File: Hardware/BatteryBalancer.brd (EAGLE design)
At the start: 49 parts, among them J2 ICSP, U3 SINGLECELL, U4 ATMEGA328P_TQFP, U5 SINGLECELL, U6 SINGLECELL, U7 SINGLECELL, Y1 16MHz

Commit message: Going home
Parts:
- removed JP10: JP10, SparkFun-Connectors:1X08_SMD_COMBINED
- removed JP11: IOL, SparkFun-Connectors:1X08_SMD_COMBINED
- removed JP13: AD, SparkFun-Connectors:1X06_SMD_STRAIGHT_COMBO
- removed U3, U5, U6, U7: SINGLECELL, BBLib:1X02_SMD_0.1IN
- added C11, C12, C13, C14, C18: 0.1uF, SparkFun-Capacitors:0603
- added C15: 10uF, SparkFun-Capacitors:EIA3216
- added C17: 10nF, SparkFun-Capacitors:0603
- added D2: GREEN, SparkFun-LED:LED-1206
- added D3: YELLOW, SparkFun-LED:LED-1206-HIDDENSILK
- added F1: 6V 0.5A, SparkFun-Fuses:0805
- added J1: (no value), SparkFun-Connectors:USB-MICROB-PTH-MILL
- added LED1: Blue, SparkFun-LED:LED-1206-HIDDENSILK
- added R1, R24: 10k, SparkFun-Resistors:0603
- added R25, R26: 4.7k, SparkFun-Resistors:0603
- added U1: CH340C, SparkFun-IC-Comms:SO016
- added U10, U11, U2, U8, U9: TAP_POINT, BBLib:1X01_SMD_0.1IN
- J2: value ICSP -> ISP
- R3: value 10k -> 4.7k
- S1: value RESET -> Tall Switch; device SparkFun-Electromechanical:TACTILE-SWITCH-SMD -> SparkFun-Switches:TACTILE_SWITCH_SMD_5.2MM
- moved S1 249.6 mm to (-80.6, -298.2)
- moved R3 249.5 mm to (-82.7, -307.2)
- moved U4 247.3 mm to (-79.4, -261.5)
- moved Y1 245.6 mm to (-60.8, -296.8)
- moved C2 241.5 mm to (-69.7, -303.4)
- moved J2 229.0 mm to (-2.54, -323.9)
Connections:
- removed net 3.3V: JP10.5A, JP10.5B
- removed net 5V: C2.2, J2.2, JP10.4A, JP10.4B, JP10.7A, JP10.7B, R3.2, U4.18, U4.4, U4.6
- removed net AD0: JP13.1A, JP13.1B, U4.23
- removed net AD1: JP13.2A, JP13.2B, U4.24
- removed net AD2: JP13.3A, JP13.3B, U4.25
- removed net AD3: JP13.4A, JP13.4B, U4.26
- removed net AD4/SDA: JP13.5A, JP13.5B, U4.27
- removed net AD5/SCL: JP13.6A, JP13.6B, U4.28
- removed net IO2: JP11.3A, JP11.3B, U4.32
- removed net IO3: JP11.4A, JP11.4B, U4.1
- removed net IO4: JP11.5A, JP11.5B, U4.2
- removed net IO5: JP11.6A, JP11.6B, U4.9
- removed net IO6: JP11.7A, JP11.7B, U4.10
- removed net IO7: JP11.8A, JP11.8B, U4.11
- removed net IO8: U4.12
- removed net IO9: U4.13
- removed net VIN: JP10.1A, JP10.1B
- new net !DTR: C12.1, U1.13
- new net !PD: R1.1, U$2.15
- new net AREF: C2.1, U4.20
- new net D+: J1.D+, U1.5
- new net D-: J1.D-, U1.6
- new net N$1: LED1.A, R3.2
- new net N$36: D3.A, R25.1
- new net SHLD: J1.SHIELD, J1.SHIELD10, J1.SHIELD2, J1.SHIELD3, J1.SHIELD4, J1.SHIELD5, J1.SHIELD6, J1.SHIELD7, J1.SHIELD8, J1.SHIELD9
- new net USBVCC: C14.1, C15.+, F1.2
- new net VBATT: R16.2, R2.2, R7.1, U$2.16, U11.1
- new net VCC: C11.2, C18.1, J2.2, R24.2, R25.2, R26.2, U1.16, U4.18, U4.4, U4.6
- new net VUSB: C13.1, F1.1, J1.VBUS
- net GND: now also C11.1, C13.2, C14.2, C15.-, C17.2, C18.2, C2.2, J1.GND, LED1.C, U1.1, U2.1; no longer C2.1, JP10.2A, JP10.2B, JP10.3A, JP10.3B, U7.1
- net N$10: now also U8.1; no longer U6.1, U7.2
- net N$2: now also D2.A, R26.1; no longer R16.2, R2.2, R7.1, U$2.16, U5.2
- net N$23: now also R1.2
- net N$38: now also C17.1, U1.4; no longer U$2.15
- net N$6: now also U10.1; no longer U3.2, U5.1
- net N$8: now also U9.1; no longer U3.1, U6.2
- net RESET: now also C12.2, R24.1; no longer JP10.6A, JP10.6B, R3.1
- net RX-I: now also D3.C, U1.2; no longer JP11.1A, JP11.1B
- net SCLK: now also R3.1
- net TX-O: now also D2.C, U1.3; no longer JP11.2A, JP11.2B
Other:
- board outline added: 6.2 x 4.2 mm

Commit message: going home
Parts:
- added C16: 10uF, SparkFun-Capacitors:EIA3216
- added C19: 0.1uF, SparkFun-Capacitors:0603
- added C20: 47uF, SparkFun-Capacitors:PANASONIC_D
- added D1: TH, SparkFun-DiscreteSemi:SOT23-3
- added D4: MATCH, SparkFun-DiscreteSemi:SOT23-3
- added IC1: OP-AMP, SparkFun-IC-Amplifiers:SO08
- added IC3: LM1117, Testing:SOT223-ALT1
- added Q4: (no value), MTAES_V2_UniqueParts:SOT23-3
- added Q5: 4.3A/20V/54mΩ, SparkFun-DiscreteSemi:SOT23-3
- added R27: 1M, SparkFun-Resistors:0603
- added R28: 330k, SparkFun-Resistors:0603
- added R29: 715, SparkFun-Resistors:0603
- added R30: 240, SparkFun-Resistors:0603
- moved FRAME1 56.1 mm to (-67.3, -40.4)
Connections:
- removed net VBATT: R16.2, R2.2, R7.1, U$2.16, U11.1
- new net 5V: C16.+, C19.1, IC3.2, IC3.4, R30.2
- new net CHARGE: IC1.1
- new net N$39: IC3.1, R29.2, R30.1
- new net N$40: D4.3, IC1.3, R27.1
- new net N$41: D1.3, IC1.2, R28.1
- new net V_BATT: C20.+, IC1.8, IC3.3, Q5.2, R27.2, R28.2
- new net V_RAW: Q5.3, R16.2, R2.2, R7.1, U$2.16, U11.1
- net GND: now also C16.-, C19.2, C20.-, D1.1, D4.1, IC1.4, Q5.1, R29.1

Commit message: Schematic mostly done, starting layout
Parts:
- removed IC3: LM1117, Testing:SOT223-ALT1
- removed Q4: (no value), MTAES_V2_UniqueParts:SOT23-3
- removed R20, R21, R22: 10k, SparkFun-Resistors:0603
- added C21: 1.0uF, SparkFun-Capacitors:1206
- added D10, D11, D7, D8, D9: BLUE, SparkFun-LED:LED-0603
- added D5, D6: 3A/10V/280mV, SparkFun-DiscreteSemi:SOD-323
- added JP1: VCC, SparkFun-Jumpers:SMT-JUMPER_2_NC_TRACE_SILK
- added Q6: (no value), MTAES_V2_UniqueParts:SOT23-3
- added R31, R32: 1k, SparkFun-Resistors:0603
- added R33, R34, R35: 10k, SparkFun-Resistors:0603
- added R40, R41, R42, R43: DNP, SparkFun-Resistors:AXIAL-0.3
- added S2: Force Charge, SparkFun-Switches:TACTILE_SWITCH_SMD_5.2MM
- added S3: TEST, SparkFun-Switches:TACTILE_SWITCH_SMD_5.2MM
- added U$1: MCP1755, BBLib:SOT23-5
- C15, C16: value 10uF -> 1.0uF; device SparkFun-Capacitors:EIA3216 -> SparkFun-Capacitors:0603
- C20: value 47uF -> 10uF; device SparkFun-Capacitors:PANASONIC_D -> SparkFun-Capacitors:1210
- Q5: value 4.3A/20V/54mΩ -> (none)
- R1, R24: value 10k -> 1k
- R29: value 715 -> 10k
- R30: value 240 -> 10k
- moved U11 445.0 mm to (94.0, 38.1), turned to 90 degrees
- moved U10 441.6 mm to (94.0, 40.6), turned to 90 degrees
- moved U9 438.5 mm to (94.0, 43.2), turned to 90 degrees
- moved U8 435.6 mm to (94.0, 45.7), turned to 90 degrees
- moved U2 433.1 mm to (94.0, 48.3), turned to 90 degrees
- moved R19 356.1 mm to (-150.0, -581.0)
- moved R1 251.2 mm to (-147.0, -496.0)
- moved R24 204.3 mm to (-147.0, -500.0)
- moved C15 180.2 mm to (-147.3, -452.1)
- moved C20 109.5 mm to (-150.0, -556.0)
- moved C16 17.8 mm to (-144.8, -436.9)
- moved R30 17.2 mm to (-147.3, -459.7)
- moved C19 14.4 mm to (-144.8, -440.7)
- moved R29 13.0 mm to (-147.3, -455.9)
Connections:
- removed net !PD: R1.1, U$2.15
- removed net N$35: R22.2, U$2.38
- removed net SCK: J2.3
- new net !CVNST: R34.1, U$2.24, U4.22
- new net LED1: D7.A, U4.23
- new net LED2: D8.A, U4.24
- new net LED3: D9.A, U4.25
- new net LED4: D10.A, U4.26
- new net N$42: D9.C, R31.2
- new net N$43: D8.C, R24.2
- new net N$44: D7.C, R1.2
- new net TEST: D11.A, S3.1, S3.2, U4.19
- net !CS: now also R35.1
- net 5V: now also C16.1, D5.A, JP1.1, U$1.5; no longer C16.+, IC3.2, IC3.4, R30.2
- net ALERT: now also R33.1, U4.32
- net CHARGE: now also Q6.3
- net GND: now also C15.2, C16.2, C20.2, C21.2, R1.1, R19.1, R23.1, R24.1, R31.1, R32.1, U$1.2; no longer C15.-, C16.-, C20.-, R29.1
- net N$23: now also R43.P$2, U$2.38; no longer C6.1, C7.1, C8.1, R1.2, U$2.18, U$2.19, U$2.29, U$2.30
- net N$32: now also R42.P$2, U$2.37; no longer R19.2, U$2.35
- net N$33: now also R41.P$2; no longer R20.2
- net N$34: now also R40.P$2, U$2.35; no longer R21.2, U$2.37
- net N$37: now also D11.C, R19.2; no longer U$2.24
- net N$39: now also D10.C, R32.2; no longer IC3.1, R29.2, R30.1
- net N$40: now also S2.1, S2.2
- net RESET: now also Q6.2, R29.1, U$1.3, U$2.15; no longer R24.1
- net SCLK: now also J2.3
- net USBVCC: now also C15.1, D6.A; no longer C15.+
- net VCC: now also D5.C, D6.C, JP1.2, Q6.1, R29.2, R33.2, R34.2, R35.2, S3.3, S3.4; no longer R24.2
- net VREG: now also C6.1, C7.1, C8.1, R40.P$1, R41.P$1, R42.P$1, R43.P$1, U$2.18, U$2.19, U$2.29, U$2.30; no longer R19.1, R20.1, R21.1, R22.1, R23.1
- net V_BATT: now also R30.2, S2.3, S2.4, U$1.1; no longer C20.+, IC3.3
- net V_RAW: now also C20.1, C21.1

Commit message: Routed 90%
Needs finishing routing and also pretty graphics
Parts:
- removed C15: 1.0uF, SparkFun-Capacitors:0603
- removed D10, D11: BLUE, SparkFun-LED:LED-0603
- removed F1: 6V 0.5A, SparkFun-Fuses:0805
- removed LED1: Blue, SparkFun-LED:LED-1206-HIDDENSILK
- removed Q10: (no value), MTAES_V2_UniqueParts:SOT23-3
- removed R34, R35: 10k, SparkFun-Resistors:0603
- removed R40, R41, R42, R43: DNP, SparkFun-Resistors:AXIAL-0.3
- removed U$1: MCP1755, BBLib:SOT23-5
- removed U$2: AD7280A, BBLib:LQFP-48
- removed U8, U9: TAP_POINT, BBLib:1X01_SMD_0.1IN
- added JP2: RPP_BYP, SparkFun-Jumpers:SMT-JUMPER_2_NC_TRACE_SILK
- added Q4: (no value), MTAES_V2_UniqueParts:SOT23-3
- added R20, R21, R22: DNP, BBLib:AXIAL-0.3
- added U12: ATMEGA328P_TQFP, SparkFun-IC-Microcontroller:TQFP32-08
- added U13: CH340C, SparkFun-IC-Comms:SO016
- added U3, U5: TAP_POINT, BBLib:1X01_SMD_0.1IN
- C1: value 0.1uF -> 10uF; device SparkFun-Capacitors:0603 -> SparkFun-Capacitors:1210
- C10, C16, C6: value 1.0uF -> 0.1uF
- C11, C13, C19, C7: value 0.1uF -> 1.0uF
- C17: value 10nF -> 0.1uF
- C2: value 0.1uF -> 1.0uF; device SparkFun-Capacitors:0603 -> SparkFun-Capacitors:1206
- C20: value 10uF -> 0.1uF; device SparkFun-Capacitors:1210 -> SparkFun-Capacitors:0603
- C21: value 1.0uF -> 10nF; device SparkFun-Capacitors:1206 -> SparkFun-Capacitors:0603
- D1: value TH -> MATCH
- D2: value GREEN -> TH; device SparkFun-LED:LED-1206 -> SparkFun-DiscreteSemi:SOT23-3
- D3: value YELLOW -> 3A/10V/280mV; device SparkFun-LED:LED-1206-HIDDENSILK -> SparkFun-DiscreteSemi:SOD-323
- D4: value MATCH -> BLUE; device SparkFun-DiscreteSemi:SOT23-3 -> SparkFun-LED:LED-0603
- D5, D6: value 3A/10V/280mV -> BLUE; device SparkFun-DiscreteSemi:SOD-323 -> SparkFun-LED:LED-0603
- D9: value BLUE -> 3A/10V/280mV; device SparkFun-LED:LED-0603 -> SparkFun-DiscreteSemi:SOD-323
- Q1: device MTAES_V2_UniqueParts:SOT23-3 -> SparkFun-DiscreteSemi:SOT23-3
- Q5: device SparkFun-DiscreteSemi:SOT23-3 -> MTAES_V2_UniqueParts:SOT23-3
- R1: value 1k -> 10; device SparkFun-Resistors:0603 -> SparkFun-Resistors:1206
- R10: value 10k -> 1M
- R15: value 10k -> 330k
- R19: value 10k -> DNP; device SparkFun-Resistors:0603 -> BBLib:AXIAL-0.3
- R24: value 1k -> 10k
- R25, R26: value 4.7k -> 10k
- R27: value 1M -> 10k
- R28: value 330k -> 10k
- R3: value 4.7k -> 10; device SparkFun-Resistors:0603 -> SparkFun-Resistors:1206
- R30, R33: value 10k -> 1k
- R5, R6: value 10 -> 10k; device SparkFun-Resistors:1206 -> SparkFun-Resistors:0603
- S1: value Tall Switch -> Force Charge
- S2: value Force Charge -> TEST
- S3: value TEST -> Tall Switch
- U1: value CH340C -> TAP_POINT; device SparkFun-IC-Comms:SO016 -> BBLib:1X01_SMD_0.1IN
- U10: value TAP_POINT -> MCP1755; device BBLib:1X01_SMD_0.1IN -> BBLib:SOT23-5
- U11: value TAP_POINT -> AD7280A; device BBLib:1X01_SMD_0.1IN -> BBLib:LQFP-48
- U4: value ATMEGA328P_TQFP -> TAP_POINT; device SparkFun-IC-Microcontroller:TQFP32-08 -> BBLib:1X01_SMD_0.1IN
- moved R19 657.3 mm to (59.4, 42.1)
- moved C21 628.5 mm to (21.0, 43.8)
- moved C20 616.9 mm to (15.7, 38.2), turned to 90 degrees
- moved R31 591.8 mm to (64.1, 48.9), turned to 180 degrees
- moved R32 587.3 mm to (39.4, 48.9), turned to 180 degrees
- moved R33 583.5 mm to (14.0, 48.9), turned to 180 degrees
- moved R1 581.6 mm to (88.9, 35.6)
- moved R24 564.1 mm to (39.1, 32.5), turned to 315 degrees
- moved D7 562.6 mm to (36.2, 48.9)
- moved R30 560.8 mm to (88.9, 48.9), turned to 180 degrees
- moved S3 559.8 mm to (52.8, 46.2)
- moved D8 557.7 mm to (10.8, 48.9)
- moved D9 548.4 mm to (14.7, 35.1), turned to 180 degrees
- moved D5 544.6 mm to (85.7, 48.9)
- moved D6 538.6 mm to (61.0, 48.9)
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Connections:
- removed net N$1: LED1.A, R3.2
- removed net N$2: D2.A, R26.1
- removed net N$36: D3.A, R25.1
- removed net VUSB: C13.1, F1.1, J1.VBUS
- net !CS: now also R28.1, U11.21, U12.14; no longer R35.1, U$2.21, U4.14
- net !CVNST: now also R27.1, U11.24, U12.22; no longer R34.1, U$2.24, U4.22
- net !DTR: now also C14.1, U13.13; no longer C12.1, U1.13
- net 5V: now also C7.1, C8.1, D3.A, U10.5; no longer C16.1, C19.1, D5.A, U$1.5
- net ALERT: now also R29.1, U11.27, U12.32; no longer R33.1, U$2.27, U4.32
- net AREF: now also C16.1, U12.20; no longer C2.1, U4.20
- net CHARGE: now also R24.1
- net D+: now also U13.5; no longer U1.5
- net D-: now also U13.6; no longer U1.6
- net GND: now also C1.2, C11.2, C12.2, C17.1, D2.1, Q1.1, Q5.2, R26.1, R30.1, R33.1, R9.1, S3.1, S3.2, U10.2, U11.17, U11.20, U11.28, U11.31, U11.41, U12.21, U12.3, U12.5, U13.1, U5.1; no longer C11.1, C14.2, C15.2, C17.2, C6.2, D4.1, LED1.C, Q3.2, Q5.1, R1.1, R15.1, R19.1, R24.1, S1.1, S1.2, U$1.2, U$2.17, U$2.20, U$2.28, U$2.31, U$2.41, U1.1, U2.1, U4.21, U4.3, U4.5
- net LED1: now also D5.A, U12.23; no longer D7.A, U4.23
- net LED2: now also D6.A, U12.24; no longer D8.A, U4.24
- net LED3: now also D7.A, U12.25; no longer D9.A, U4.25
- net LED4: now also D8.A, U12.26; no longer D10.A, U4.26
- net MISO: now also U11.26, U12.16; no longer U$2.26, U4.16
- net MOSI: now also U11.23, U12.15; no longer U$2.23, U4.15
- net N$10: now also Q4.2, R4.2, R8.1, U4.1; no longer Q2.2, R10.1, R6.2, U8.1
- net N$11: now also Q5.3, R4.1; no longer Q3.3, R6.1
- net N$12: now also Q2.1; no longer Q10.1
- net N$13: now also Q3.1; no longer Q1.1
- net N$14: now also U11.14; no longer U$2.14
- net N$15: now also Q4.1; no longer Q2.1
- net N$16: now also Q5.1; no longer Q3.1
- net N$17: now also C6.2, R9.2, U11.13; no longer C1.2, R15.2, U$2.13
- net N$18: now also U11.12; no longer U$2.12
- net N$19: now also C5.2, C6.1, R8.2, U11.11; no longer C1.1, C3.2, R10.2, U$2.11
- net N$20: now also U11.10; no longer U$2.10
- net N$21: now also C5.1, R7.2, U11.9; no longer C3.1, R9.2, U$2.9
- net N$22: now also U11.8; no longer U$2.8
- net N$23: now also R22.P$2, U11.38; no longer R43.P$2, U$2.38
- net N$24: now also U11.6; no longer U$2.6
- net N$25: now also C3.1, R5.2, U11.1; no longer C5.1, R7.2, U$2.1
- net N$26: now also C3.2, R6.2, U11.3, U11.5, U11.7; no longer C5.2, R8.2, U$2.3, U$2.5, U$2.7
- net N$27: now also U11.40; no longer U$2.40
- net N$28: now also U11.33; no longer U$2.33
- net N$29: now also C11.1, U11.39; no longer C10.1, U$2.39
- net N$3: now also U12.7; no longer U4.7
- net N$30: now also U11.32; no longer U$2.32
- net N$31: now also U11.34; no longer U$2.34
- net N$32: now also R21.P$2, U11.37; no longer R42.P$2, U$2.37
- net N$33: now also R20.P$2, U11.36; no longer R41.P$2, U$2.36
- net N$34: now also R19.P$2, U11.35; no longer R40.P$2, U$2.35
- net N$37: now also D4.C, R26.2; no longer D11.C, R19.2
- net N$38: now also C21.1, U13.4; no longer C17.1, U1.4
- net N$39: now also D8.C, R33.2; no longer D10.C, R32.2
- net N$4: now also U12.8; no longer U4.8
- net N$40: now also D1.3, R10.1, S1.1, S1.2; no longer D4.3, R27.1, S2.1, S2.2
- net N$41: now also D2.3, R15.1; no longer D1.3, R28.1
- net N$42: now also D7.C, R32.2; no longer D9.C, R31.2
- net N$43: now also D6.C, R31.2; no longer D8.C, R24.2
- net N$44: now also D5.C, R30.2; no longer D7.C, R1.2
- net N$5: now also Q2.3, R1.1; no longer Q10.3, R2.1
- net N$6: now also Q2.2, R2.2, R6.1, U2.1; no longer Q10.2, R4.2, R8.1, U10.1
- net N$7: now also Q3.3, R2.1; no longer Q1.3, R4.1
- net N$8: now also Q3.2, R3.2, R7.1, U3.1; no longer Q1.2, R5.2, R9.1, U9.1
- net N$9: now also Q4.3, R3.1; no longer Q2.3, R5.1
- net RESET: now also C14.2, R25.1, S3.3, S3.4, U10.3, U11.15, U12.29; no longer C12.2, R29.1, S1.3, S1.4, U$1.3, U$2.15, U4.29
- net RX-I: now also U12.30, U13.2; no longer D3.C, U1.2, U4.30
- net SCLK: now also U11.22, U12.17; no longer R3.1, U$2.22, U4.17
- net TEST: now also D4.A, S2.1, S2.2, U12.1; no longer D11.A, S3.1, S3.2, U4.19
- net TX-O: now also U12.31, U13.3; no longer D2.C, U1.3, U4.31
- net USBVCC: now also C18.1, C19.1, D9.A, J1.VBUS; no longer C14.1, C15.1, D6.A, F1.2
- net VCC: now also C17.2, C20.1, D3.C, D9.C, R27.2, R28.2, S2.3, S2.4, U12.18, U12.4, U12.6, U13.16; no longer C11.2, C18.1, D5.C, D6.C, R26.2, R33.2, R34.2, R35.2, S3.3, S3.4, U1.16, U4.18, U4.4, U4.6
- net VREG: now also C10.1, C12.1, C13.1, R19.P$1, R20.P$1, R21.P$1, R22.P$1, U11.18, U11.19, U11.29, U11.30; no longer C6.1, C7.1, C8.1, R40.P$1, R41.P$1, R42.P$1, R43.P$1, U$2.18, U$2.19, U$2.29, U$2.30
- net V_BATT: now also JP2.2, Q1.2, R10.2, R15.2, R24.2, S1.3, S1.4, U10.1; no longer Q5.2, R27.2, R28.2, R30.2, S2.3, S2.4, U$1.1
- net V_RAW: now also C1.1, C2.1, JP2.1, Q1.3, R1.2, R5.1, U1.1, U11.16; no longer C20.1, C21.1, Q5.3, R2.2, R7.1, U$2.16, U11.1
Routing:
- net VCC: track 0.00 -> 95.6 mm, vias 0 -> 5
- net RESET: track 0.00 -> 89.9 mm, vias 0 -> 5
- net V_BATT: track 0.00 -> 75.6 mm, vias 0 -> 2
- net LED1: track 0.00 -> 52.6 mm
- net ALERT: track 0.00 -> 50.1 mm, vias 0 -> 4
- net VREG: track 0.00 -> 49.9 mm
- net SCLK: track 0.00 -> 49.4 mm, vias 0 -> 1
- net !CVNST: track 0.00 -> 46.5 mm, vias 0 -> 2
- net V_RAW: track 0.00 -> 46.2 mm
- net !CS: track 0.00 -> 45.5 mm, vias 0 -> 2
- net MOSI: track 0.00 -> 42.0 mm, vias 0 -> 1
- net MISO: track 0.00 -> 39.4 mm, vias 0 -> 1
- net LED4: track 0.00 -> 33.5 mm, vias 0 -> 2
- net N$40: track 0.00 -> 33.2 mm
- net LED2: track 0.00 -> 31.3 mm, vias 0 -> 2
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- added copper zone on layer 1, net GND
- added copper zone on layer 16, net GND
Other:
- board size 6.2 x 4.2 mm -> 4.2 x 6.2 mm

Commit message: Did a DRC check
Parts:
- moved C17 1.27 mm to (41.1, 43.8)
- moved C16 1.02 mm to (40.1, 45.0)
- moved C6 0.77 mm to (78.9, 45.8)
- moved R9 0.76 mm to (80.3, 45.8)
- moved R18 0.63 mm to (59.9, 45.5)
- moved C5 0.52 mm to (78.9, 42.5)
- moved R8 0.51 mm to (80.3, 42.5)
- moved C12 0.40 mm to (65.4, 46.1)
- moved R17 0.38 mm to (61.5, 45.5)
- moved C4 0.28 mm to (78.9, 39.2)
- moved R7 0.25 mm to (80.3, 39.2)
- moved C10 0.25 mm to (75.3, 46.7)
- moved C18 0.25 mm to (14.7, 32.1)
- moved C3 0.13 mm to (78.9, 35.9)
- moved C1 0.13 mm to (88.9, 32.9)
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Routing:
- net SHLD: track 0.00 -> 5.46 mm, vias 0 -> 1
- net V_BATT: track 75.6 -> 71.7 mm, vias 2 -> 4
- net N$17: track 5.82 -> 7.96 mm
- net LED1: track 52.6 -> 53.7 mm
- net GND: track 24.2 -> 25.1 mm, vias 34 -> 37
- net N$21: track 8.02 -> 8.70 mm
- net AREF: track 3.10 -> 3.78 mm
- net VCC: track 95.6 -> 96.2 mm
- net !CVNST: track 46.5 -> 47.0 mm
- added copper zone on layer 1, net SHLD
- added copper zone on layer 16, net SHLD
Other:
- board size 4.2 x 6.2 mm -> 93.6 x 20.1 mm

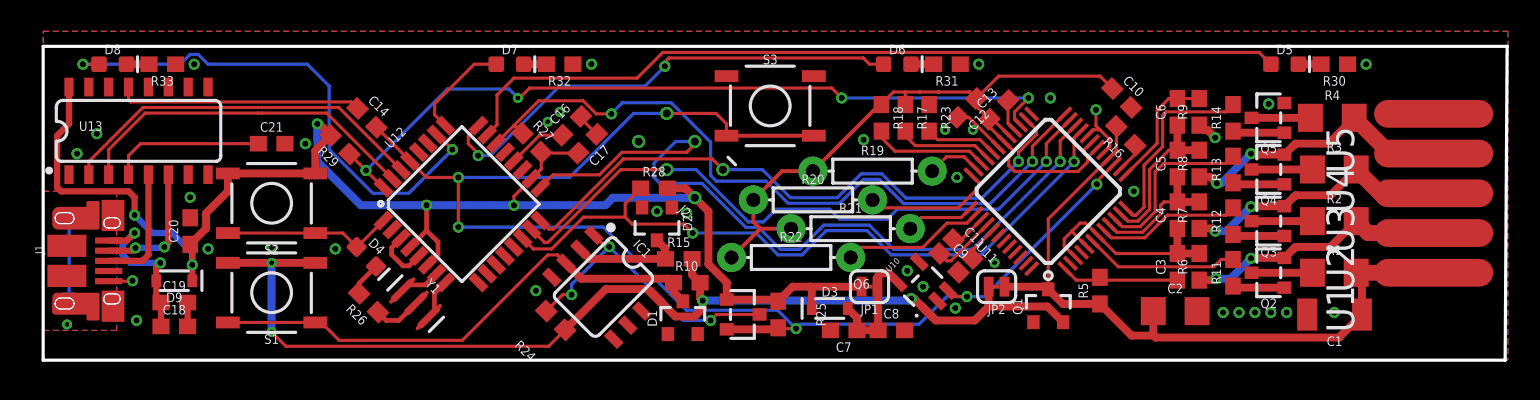
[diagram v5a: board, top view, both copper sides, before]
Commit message: Add spacious test board design
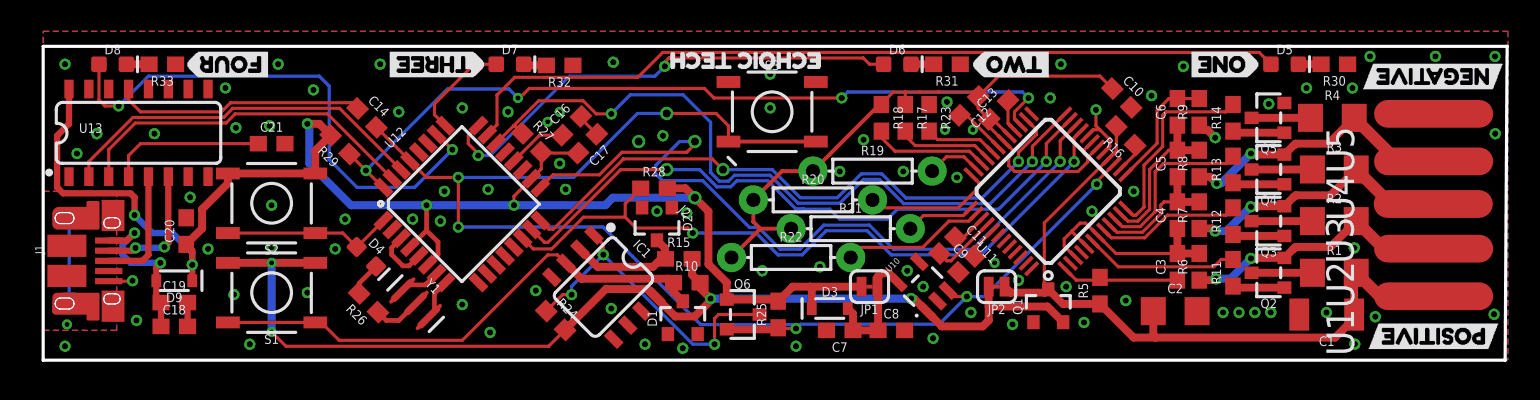
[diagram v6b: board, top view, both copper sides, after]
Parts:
- added U$1: (no value), buzzard_labels_0:POSITIVE1
- added U$2: (no value), buzzard_labels_0:NEGATIVE0
- added U$3: (no value), buzzard_labels_0:ONE3
- added U$4: (no value), buzzard_labels_0:TWO4
- added U$5: (no value), buzzard_labels_0:THREE6
- added U$6: (no value), buzzard_labels_0:FOUR5
- added U$7: (no value), buzzard_labels_0:ECHOIC_TECH7
- moved U1 1.50 mm to (95.2, 34.1)
- moved U2 1.00 mm to (95.2, 37.1)
- moved U3 0.68 mm to (95.2, 40.0)
- moved C1 0.50 mm to (88.4, 32.9)
- moved U4 0.50 mm to (95.2, 42.7)
- moved S3 0.40 mm to (53.0, 45.9)
- moved C20 0.25 mm to (15.5, 38.2)
- moved C7 0.25 mm to (57.3, 31.9)
- moved C11 0.18 mm to (65.3, 37.2)
- moved C12 0.18 mm to (65.5, 46.2)
- moved U13 0.13 mm to (12.4, 44.5)
- moved R32 0.08 mm to (39.4, 48.8)
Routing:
- net CHARGE: track 19.1 -> 21.1 mm
- net !CVNST: track 47.0 -> 48.4 mm
- net VCC: track 96.2 -> 97.6 mm
- net V_RAW: track 46.4 -> 47.1 mm
- net GND: track 25.1 -> 24.5 mm, vias 37 -> 89
